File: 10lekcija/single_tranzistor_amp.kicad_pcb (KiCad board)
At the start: 2 copper layers, 31.2 x 25.7 mm, 11 parts, among them P1 PWR_CONN, P2 SIGNAL_IN, P3 SIGNAL_OUT, Q1 BC548

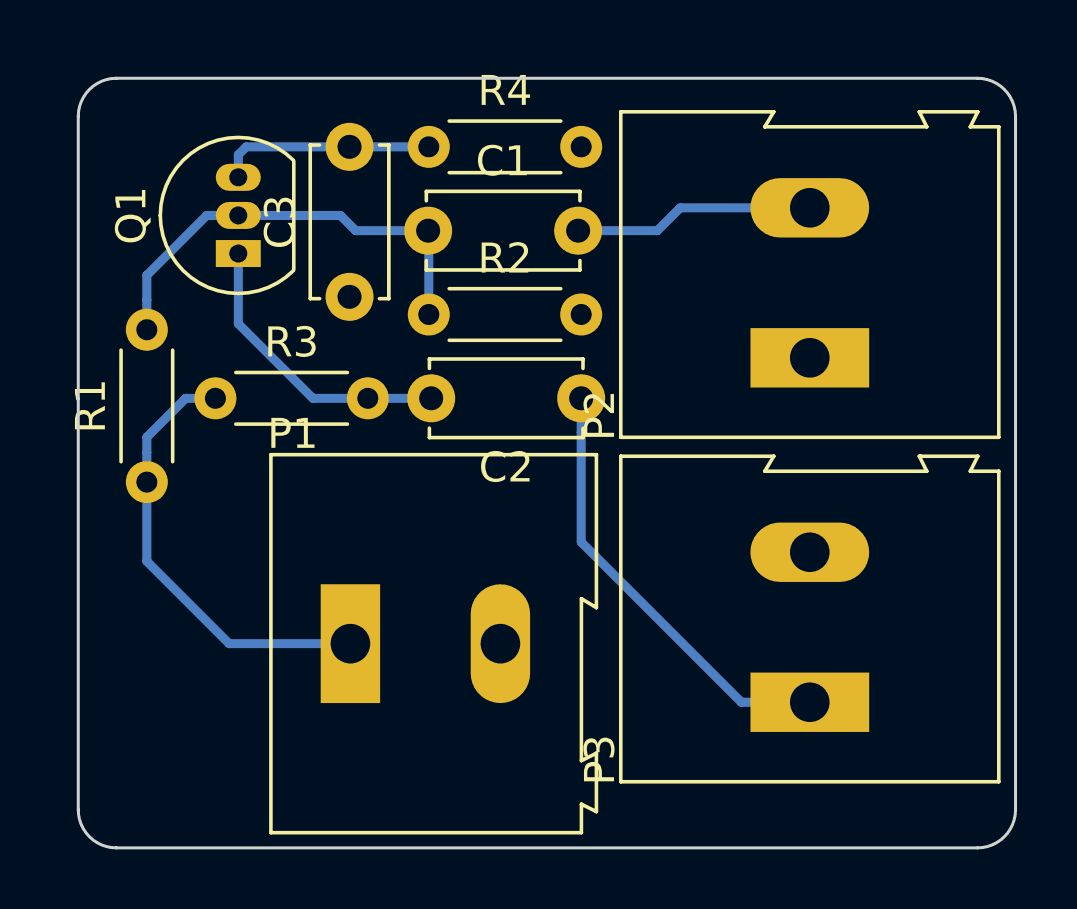
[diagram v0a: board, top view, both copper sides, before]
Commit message: Kursa darba papildinajums, lekciju darbu nobeigums
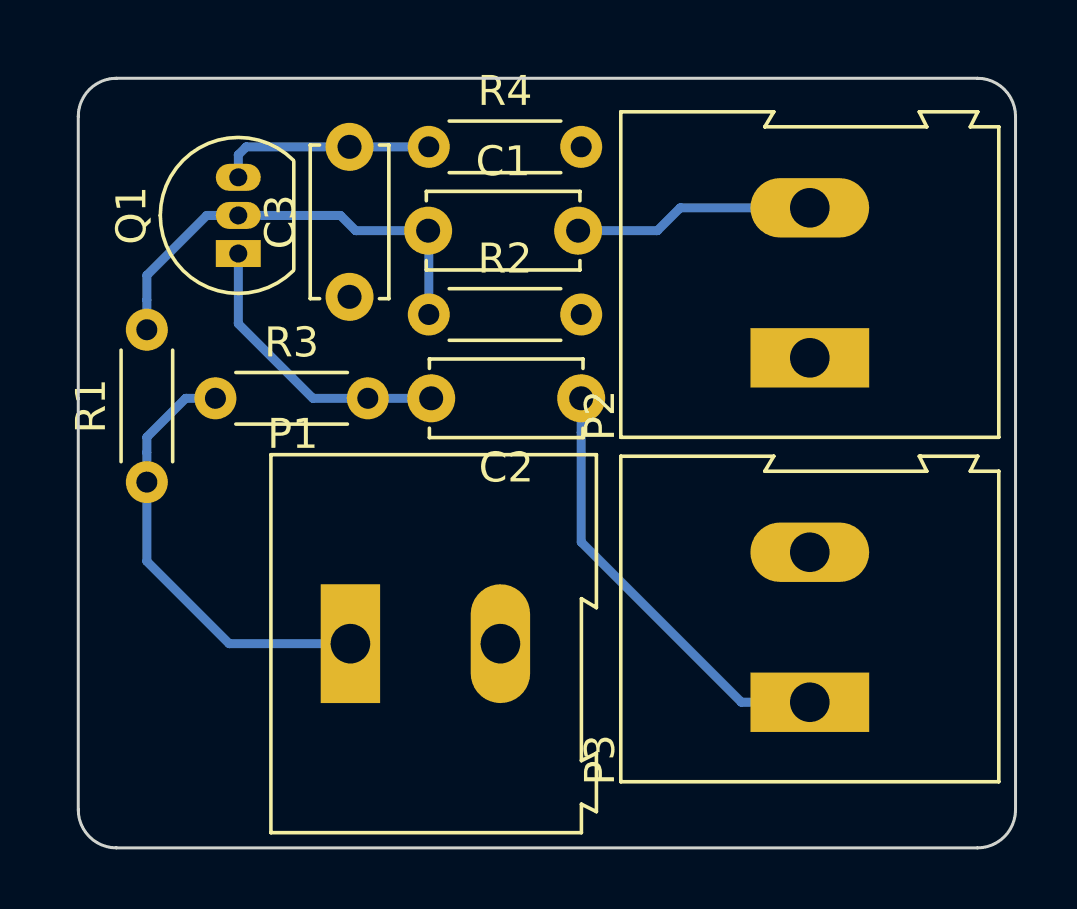
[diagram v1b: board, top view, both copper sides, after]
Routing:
- added copper zone on F.Cu, net GND
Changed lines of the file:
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@@
   (general
     (links 16)
-    (no_connects 10)
-    (area 164.287999 83.007999 195.630001 108.762001)
+    (no_connects 0)
+    (area 163.489 82.209 197.847 111.0298)
     (thickness 1.6)
     (drawings 12)
@@
     (visible_elements 7FFFEFDF)
     (pcbplotparams
-      (layerselection 0x00030_80000001)
+      (layerselection 0x010a0_80000001)
       (usegerberextensions false)
       (excludeedgelayer true)
@@
       (psa4output false)
       (plotreference true)
-      (plotvalue true)
+      (plotvalue false)
       (plotinvisibletext false)
       (padsonsilk false)
@@
       (outputformat 1)
       (mirror false)
-      (drillshape 1)
+      (drillshape 0)
       (scaleselection 1)
       (outputdirectory ""))
@@
     (connect_pads (clearance 0.508))
     (min_thickness 0.254)
+    (fill yes (mode segment) (arc_segments 32) (thermal_gap 0.508) (thermal_bridge_width 0.508))
+    (polygon
+      (pts
+        (xy 194.31 108.712) (xy 194.564 108.712) (xy 195.072 108.458) (xy 195.326 108.204) (xy 195.58 107.696)
+        (xy 195.58 107.442) (xy 195.58 84.074) (xy 195.326 83.566) (xy 195.072 83.312) (xy 194.564 83.058)
+        (xy 165.354 83.058) (xy 164.846 83.312) (xy 164.592 83.566) (xy 164.338 84.074) (xy 164.338 107.696)
+        (xy 164.592 108.204) (xy 164.846 108.458) (xy 165.354 108.712)
+      )
+    )
+  )
+  (zone (net 5) (net_name GND) (layer F.Cu) (hatch edge 0.508)
+    (connect_pads (clearance 0.508))
+    (min_thickness 0.254)
